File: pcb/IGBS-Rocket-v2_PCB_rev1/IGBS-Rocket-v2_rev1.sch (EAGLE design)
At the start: 157 parts, among them Q1 BC817, Q2 ENC-03, U1 STM32H750VBT6, U2 LD1085D2M-R, U3 LD1085D2M-R, U4 LM317SX/NOPB, U5 MICROSD, U6 ESP-12E/F, U8 LP324DRG4, U9 MCP6V51T-E/MS, Y1 24MHz

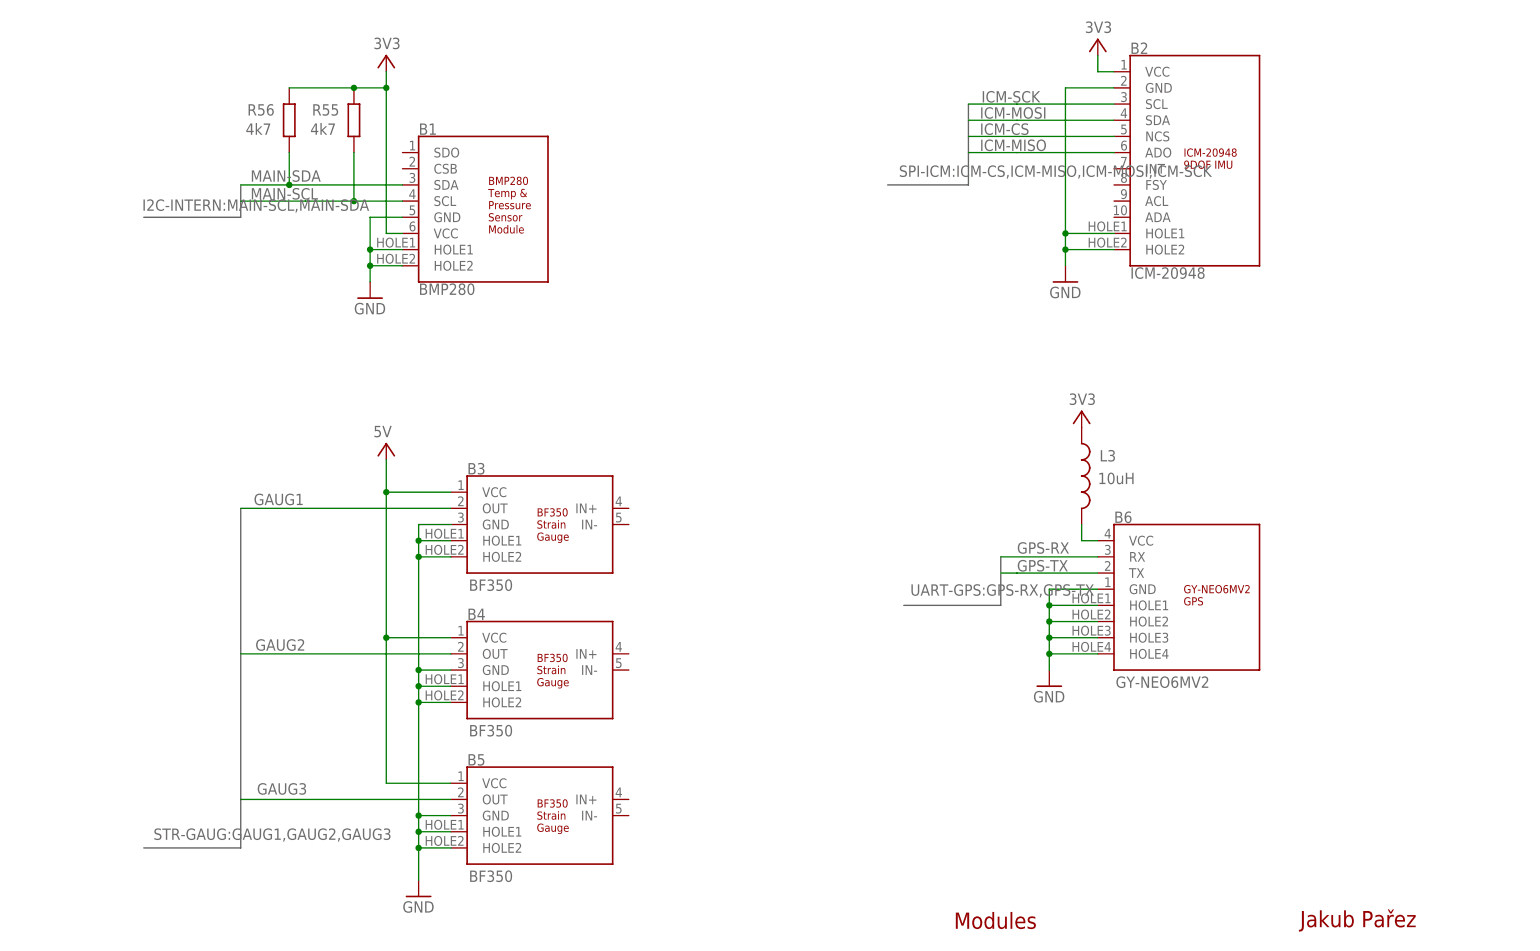
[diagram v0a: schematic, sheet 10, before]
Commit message: * schematics is validated and ready for layout
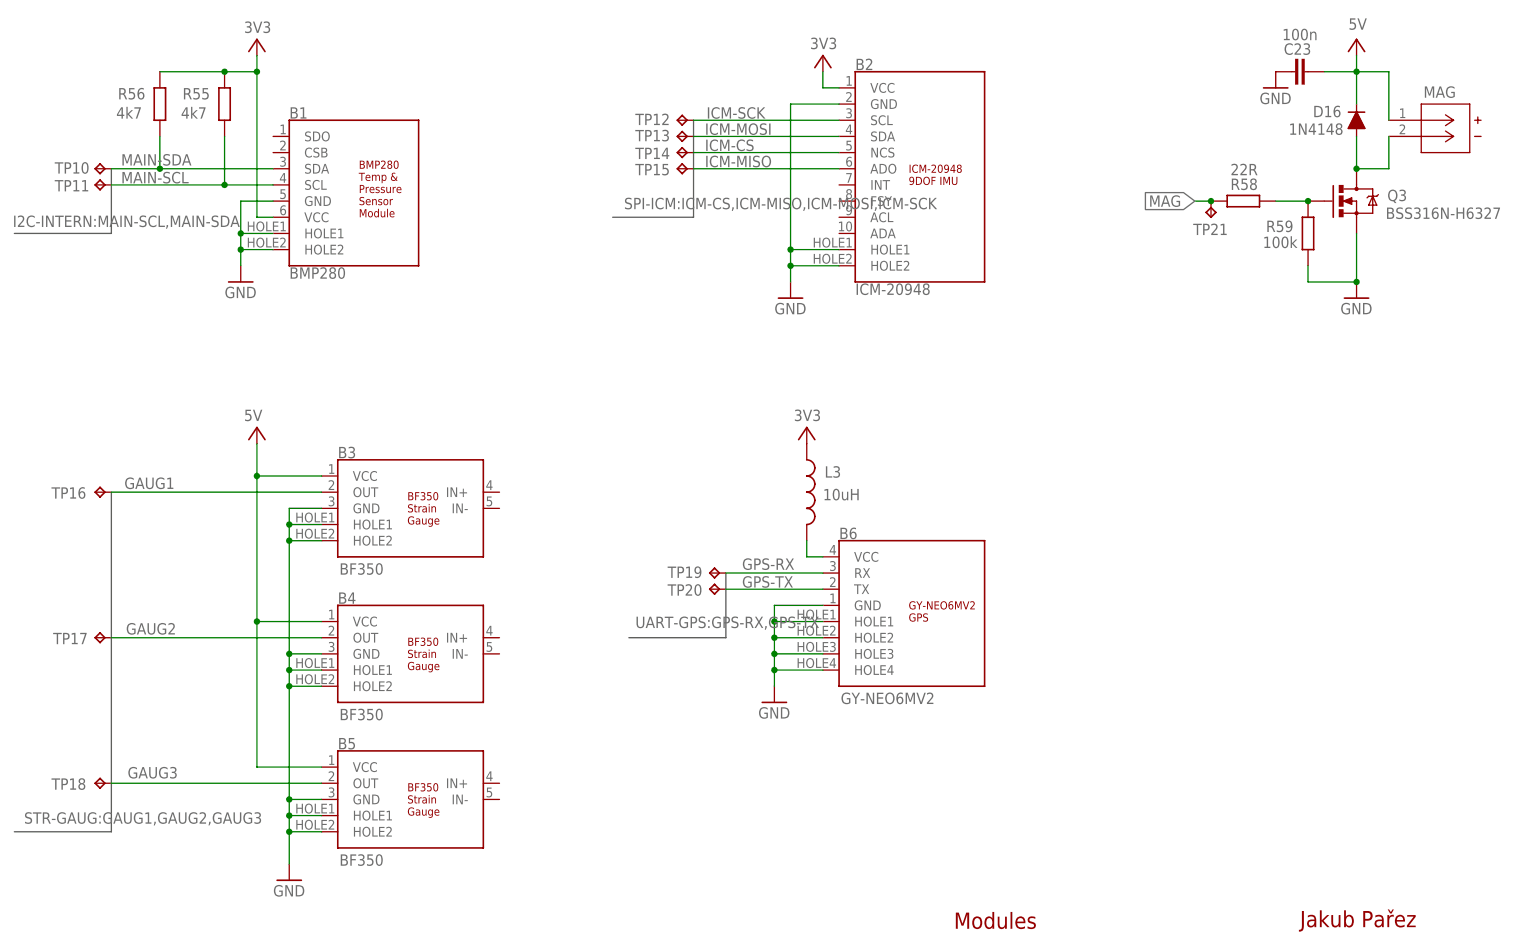
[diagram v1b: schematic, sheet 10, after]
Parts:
- removed BAT, ESP-UART: (no value), pinhead:PINHD-1X2
- removed GYRO: (no value), pinhead:PINHD-1X1
- removed SD-SPI: (no value), pinhead:PINHD-1X4
- added C23: 100n, rcl2:C-EUC0603K
- added D16: 1N4148, SparkFun-DiscreteSemi:DIODESOD123
- added Q3: BSS316N-H6327, SparkFun-DiscreteSemi:MOSFET-NCHANNELBSS123LT1G
- added R58: 22R, rcl2:R-EU_R0603
- added R59: 100k, rcl2:R-EU_R0603
- added TP1: TPB2,54, testpad:TPB2,54
- added TP10, TP11, TP12, TP13, TP14, TP15, TP16, TP17, TP18, TP19, TP2, TP20, TP21, TP3, TP4, TP5, TP6, TP7, TP8, TP9: TPB1,27, testpad:TPB1,27
- MAG: value S3B-XH-A(LF)(SN)CONN_S3B-XH-A(LF)(SN)_JST -> S2B-XH-A(LF)(SN)CONN_S2B-XH-A_JST; device jst-XH2:S3B-XH-A(LF)(SN)CONN_S3B-XH-A(LF)(SN)_JST -> jst-XH2:S2B-XH-A(LF)(SN)CONN_S2B-XH-A_JST
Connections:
- new net N$43: D16.A, MAG.2, Q3.D
- new net N$44: Q3.G, R58.2, R59.2
- net 5V: now also C23.1, D16.C
- net ANG-RATE: now also TP9.TP; no longer GYRO.1
- net BAT: now also TP1.TP; no longer BAT.1
- net ESP-RX: now also TP8.TP; no longer ESP-UART.2
- net ESP-TX: now also TP7.TP; no longer ESP-UART.1
- net GAUG1: now also TP16.TP
- net GAUG2: now also TP17.TP
- net GAUG3: now also TP18.TP
- net GND: now also C23.2, Q3.S, R59.1; no longer BAT.2, MAG.3
- net GPS-RX: now also TP19.TP
- net GPS-TX: now also TP20.TP
- net ICM-CS: now also TP14.TP
- net ICM-MISO: now also TP15.TP
- net ICM-MOSI: now also TP13.TP
- net ICM-SCK: now also TP12.TP
- net MAG: now also R58.1, TP21.TP; no longer MAG.2
- net MAIN-SCL: now also TP11.TP
- net MAIN-SDA: now also TP10.TP
- net SD-CLK: now also TP4.TP; no longer SD-SPI.2
- net SD-CS: now also TP2.TP; no longer SD-SPI.4
- net SD-DETECT: now also TP6.TP
- net SD-MISO: now also TP5.TP; no longer SD-SPI.1
- net SD-MOSI: now also TP3.TP; no longer SD-SPI.3
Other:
- note added: "MAGNET"
- moved on the sheet: 5V, B1, B2, B3, B4, B5, B6, L3, R55, R56

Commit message: + PCB - BOM created * minor adjustments to PCB schematics
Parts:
- removed C32, C34, C37: 10u, rcl2:CPOL-EUCT3216
- removed ON-OFF: (no value), switch_btn:255SB
- added C24, C30, C31: 10u, SparkFun-Capacitors:10UF10V10%(0805)
- 3V3, 5V, I2C-AUX, UART-AUX: device pinhead:PINHD-1X2 -> pinhead2:PINHD-1X2
- ADC-AUX, SPI-AUX: device pinhead:PINHD-1X3 -> pinhead2:PINHD-1X3
- C19, C3, C5, C7, C9: device rcl2:CPOL-EUCT3216 -> SparkFun-Capacitors:10UF10V10%(0805)
- C2: value 2n2 Y2 -> 10u; device rcl2:C-EUC2220K -> SparkFun-Capacitors:10UF10V10%(0805)
- D14: value 3V6 5uA -> 3V6
- GND-AUX, GPIO-AUX: device pinhead:PINHD-1X4 -> pinhead2:PINHD-1X4
- H1, H2, H3, H4: value MOUNT-PAD-ROUND3.0 -> MOUNT-PAD-ROUND2.8; device holes:MOUNT-PAD-ROUND3.0 -> holes:MOUNT-PAD-ROUND2.8
- PPTC1: value 8A -> 6V/2A
- R11, R12, R13, R14, R19, R20, R21, R22, R23, R24, R25, R26, R27, R28, R29, R44, R45, R46, R47, R54: device rcl2:R-EU_R0805 -> rcl2:R-EU_R0603
- SWD: device pinhead:PINHD-1X6 -> pinhead2:PINHD-1X6
- TP1: device testpad:TPB2,54 -> testpad2:TPB2,54
- TP10, TP11, TP12, TP13, TP14, TP15, TP16, TP17, TP18, TP19, TP2, TP20, TP21, TP3, TP4, TP5, TP6, TP7, TP8, TP9: device testpad:TPB1,27 -> testpad2:TPB1,27
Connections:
- net LED1-RED renamed LED1-BLUE
- net LED2-GREEN renamed LED2-YELLOW
- net LED3-BLUE renamed LED3-RED
- net LED4-ORANGE renamed LED4-WHITE
- removed net N$18: ON-OFF.S, PWR-A.+, PWR-B.1
- net 3V3: now also C31.1, C9.1; no longer C3.+, C37.+
- net 5V: now also C19.1; no longer C19.+
- net BAT: now also C2.1, C3.1, C5.1, C7.1; no longer C5.+, C7.+, C9.+
- net GND: now also C24.2, C3.2, C30.2, C31.2, C5.2, C7.2, C9.2; no longer C3.-, C32.-, C34.-, C37.-, C5.-, C7.-, C9.-
- net N$2: now also PWR-A.+, PWR-B.1; no longer C2.1, ON-OFF.P
- net N$29: now also C19.2; no longer C19.-
- net N$39: now also C24.1, C30.1; no longer C32.+, C34.+
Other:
- moved on the sheet: C2, PPTC1, PWR-A, PWR-B

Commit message: + PCB BOM
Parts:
- C16, C17, C26, C27, C28: device rcl2:C-EUC0603K -> rcl2:C-EUC0805K
- L1, L2, L3: device rcl2:INDUCTOR0603 -> rcl2:INDUCTOR0805
- R53: value 75k -> 59k

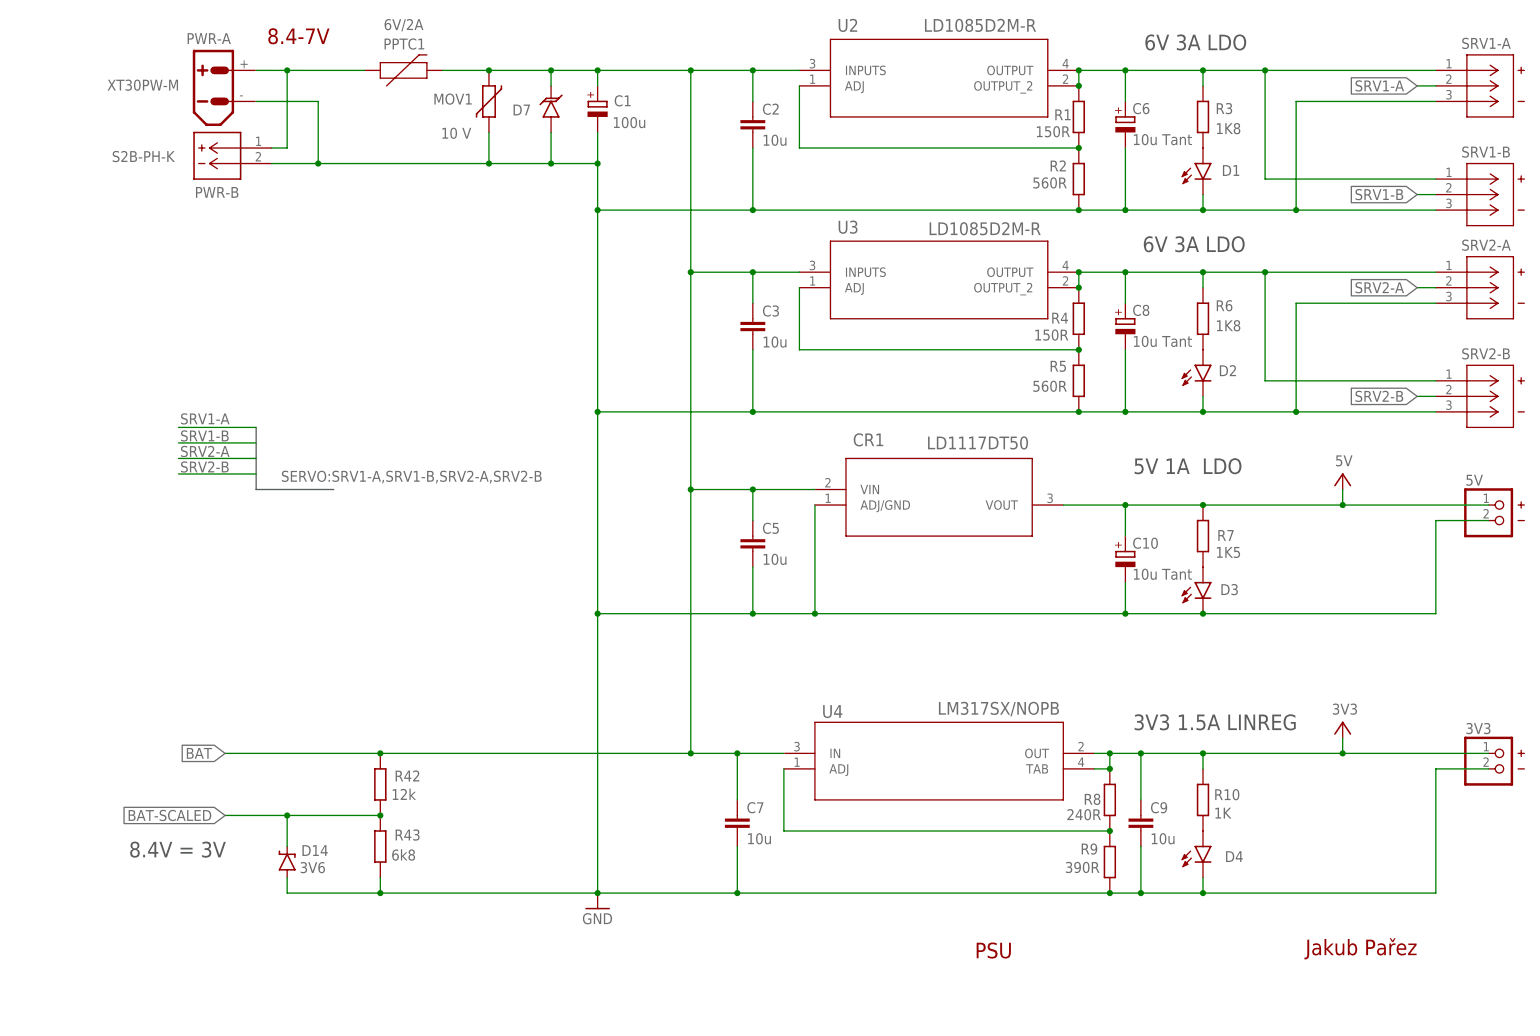
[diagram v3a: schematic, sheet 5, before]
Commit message: * PCB layout 30 % T strain-gauge modules to sch
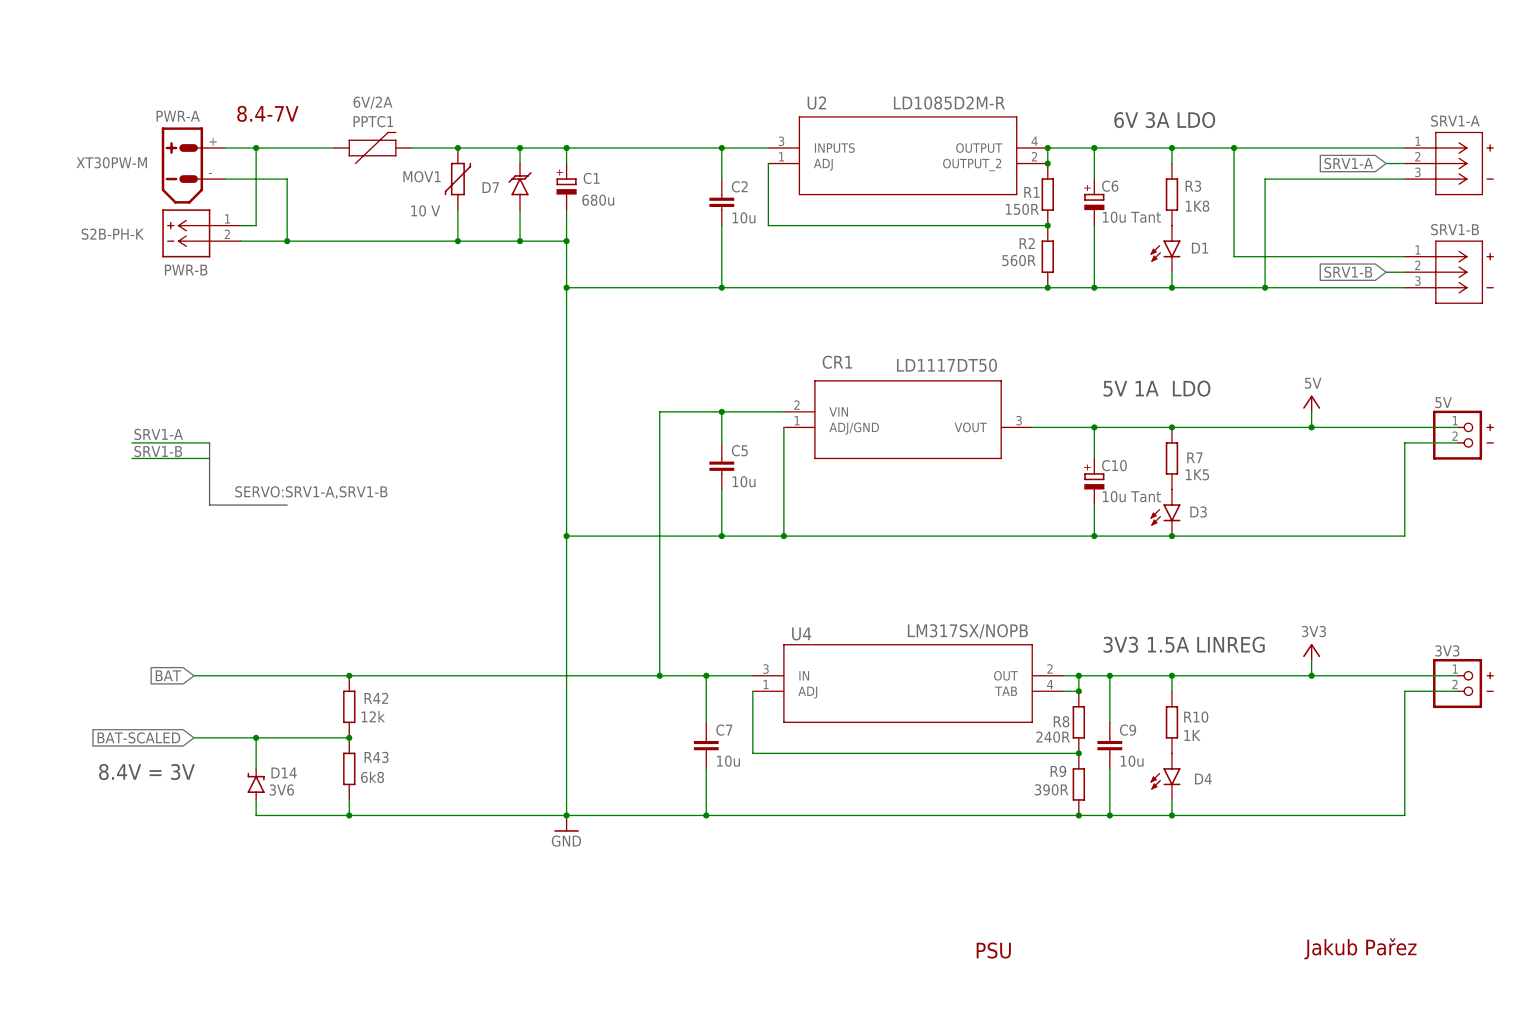
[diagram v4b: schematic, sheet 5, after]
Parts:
- removed C3: 10u, SparkFun-Capacitors:10UF10V10%(0805)
- removed C8: 10u Tant, rcl2:CPOL-EUCT3216
- removed D2: GREEN, leds:LED-GREEN1206
- removed R4: 150R, rcl2:R-EU_R0603
- removed R5: 560R, rcl2:R-EU_R0603
- removed R6: 1K8, rcl2:R-EU_R0603
- removed SRV2-A, SRV2-B: S3B-XH-A(LF)(SN)CONN_S3B-XH-A(LF)(SN)_JST, jst-XH2:S3B-XH-A(LF)(SN)CONN_S3B-XH-A(LF)(SN)_JST
- removed U3: LD1085D2M-R, ldo:LD1085D2M-RD2PAK/A_STM
- added C32: 330u, rcl2:CPOL-EUE2.5-7
- added H5, H6: MOUNT-PAD-ROUND2.8, holes:MOUNT-PAD-ROUND2.8
- added R60, R61: 1K, rcl2:R-EU_R0603
- C1: value 100u -> 680u
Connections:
- removed net 6V-2: C8.+, R4.2, R6.2, SRV2-A.1, SRV2-B.1, U3.OUTPUT, U3.OUTPUT_2
- removed net N$11: R4.1, R5.2, U3.ADJ
- removed net N$12: D2.A, R6.1
- removed net N$20: D15.C, R57.1
- removed net N$24: C21.1, RESET.1
- removed net N$25: C21.2, RESET.3
- removed net N$26: BTN1.1, C22.1
- removed net N$27: BTN1.3, C22.2
- removed net SRV2-A: SRV2-A.2, U1A.PD14
- removed net SRV2-B: SRV2-B.2, U1A.PC7
- new net BTN12: BTN1.2, R14.2, R61.1
- new net N$18: C1.+, C2.1, D7.C, MOV1.1, PPTC1.2, U2.INPUTS
- new net NRST2: R29.2, R60.1, RESET.2
- net ANG-RATE: now also D15.C, R57.1
- net BAT: no longer C1.+, C2.1, C3.1, D7.C, MOV1.1, PPTC1.2, U2.INPUTS, U3.INPUTS
- net BTN1: now also C22.1, R61.2; no longer BTN1.2, R14.2
- net GND: now also C21.2, C22.2, C32.-, H5.MOUNT, H6.MOUNT; no longer C3.2, C8.-, D2.C, R5.1, SRV2-A.3, SRV2-B.3
- net N$39: now also C32.+
- net NRST: now also C21.1, R60.2; no longer R29.2, RESET.2
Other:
- moved on the sheet: 3V3, 5V, BTN1, C1, C10, C2, C21, C22, C5, C6, C7, C9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

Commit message: + PCB schematic is DONE + BOM (Mouser) is DONE
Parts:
- removed B3, B4, B5: BF350, modules:BF350
- removed U4: LM317SX/NOPB, linreg:LM317SX/NOPBTS3B_TEX
- added C3, C35, C40: 100n, rcl2:C-EUC0603K
- added C34, C37, C38, C39, C41, C42, C43, C8: 1u, rcl2:C-EUC0603K
- added CR2, CR3, CR4: TS4040DILT-2.5, ref:TL431QDBZR,215SOT23_TO-236AB_NEX
- added CR5: AZ2185D, ldo:AZ2185D
- added D2: 3V6, SparkFun-DiscreteSemi:DIODE-ZENER16V
- added IC1, IC2, IC3: NCV21872DR2G, opamps:LM358D
- added L4: 10uH, rcl2:INDUCTOR0805
- added R4, R68, R77: 500k, trimmer:PVG3A103C01R00RES_C01R00
- added R5, R69, R78: 10k, rcl2:R-EU_R0603
- added R6, R62, R63, R70, R71, R72, R79, R80, R81: 360R, rcl2:R-EU_R0603
- added R64, R66, R73, R75, R82, R84: 470k, rcl2:R-EU_R0603
- added R65, R74, R83: 20k, rcl2:R-EU_R0603
- added R67, R76, R85: 330R, rcl2:R-EU_R0603
- added SG1, SG2, SG3: S3B-XH-A, jst-XH2:S2B-XH-A(LF)(SN)CONN_S2B-XH-A_JST
- C30: value 10u -> 1u; device SparkFun-Capacitors:10UF10V10%(0805) -> rcl2:C-EUC0603K
- CR1: device ldo:LD1117DT50TRDPAK_STM -> ldo:LD1117DT50TR
- U2: value LD1085D2M-R -> LM317BD2TG; device ldo:LD1085D2M-RD2PAK/A_STM -> linreg:LM317BD2TG
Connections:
- removed net GAUG1: B3.OUT, TP16.TP, U1A.PC5
- removed net GAUG2: B4.OUT, TP17.TP, U1A.PB0
- removed net GAUG3: B5.OUT, TP18.TP, U1A.PB1
- new net ANG-RATE2: C28.2, R53.1, R57.2, U9P.OUT
- new net N$11: R5.2, R6.1, SG1.1
- new net N$12: C8.2, IC1A.+IN, R62.1, R63.2
- new net N$20: R69.2, R70.1, SG2.1
- new net N$24: IC1A.-IN, R5.1, R64.2
- new net N$25: IC1A.OUT, R64.1, R65.2
- new net N$26: IC1B.-IN, R65.1, R66.2
- new net N$53: C34.2, IC1B.+IN, R4.2
- new net N$54: CR2.1, R4.1, R63.1, R67.1, SG1.2
- new net N$55: C37.2, IC2A.+IN, R71.1, R72.2
- new net N$56: IC2A.-IN, R69.1, R73.2
- new net N$57: IC2A.OUT, R73.1, R74.2
- new net N$58: IC2B.-IN, R74.1, R75.2
- new net N$60: C39.2, IC2B.+IN, R68.2
- new net N$61: CR3.1, R68.1, R72.1, R76.1, SG2.2
- new net N$62: R78.2, R79.1, SG3.1
- new net N$63: C41.2, IC3A.+IN, R80.1, R81.2
- new net N$64: IC3A.-IN, R78.1, R82.2
- new net N$65: IC3A.OUT, R82.1, R83.2
- new net N$66: IC3B.-IN, R83.1, R84.2
- new net N$68: C43.2, IC3B.+IN, R77.2
- new net N$69: CR4.1, R77.1, R81.1, R85.1, SG3.2
- new net SG1: C30.2, IC1B.OUT, R66.1, TP16.TP, U1A.PC5
- new net SG2: C38.2, IC2B.OUT, R75.1, TP17.TP, U1A.PB0
- new net SG3: C42.2, IC3B.OUT, R84.1, TP18.TP, U1A.PB1
- net 3V3: now also D2.C, L4.2, U2.OUT, U8A.-, U8B.-, U8C.-, U8D.-; no longer R44.2, R45.2, R46.2, R47.2, U4.OUT, U4.TAB, U8G$1.-, U8G$2.-, U8G$3.-, U8G$4.-
- net 5V: now also C3.2, C35.2, C40.2, IC1P.V+, IC2P.V+, IC3P.V+, R67.2, R76.2, R85.2, U8P.VCC, U9P.VCC; no longer B3.VCC, B4.VCC, B5.VCC, U8G$5.VCC, U9G$1.VCC
- net 6V-1: now also CR5.VOUT; no longer U2.OUTPUT, U2.OUTPUT_2
- net ANG-RATE: now also D2.A; no longer C28.2, R53.1, R57.2, U9G$1.OUT
- net BAT: now also U2.IN; no longer U4.IN
- net GND: now also C3.1, C30.1, C34.1, C35.1, C37.1, C38.1, C39.1, C40.1, C41.1, C42.1, C43.1, C8.1, CR2.2, CR2.3, CR3.2, CR3.3, CR4.2, CR4.3, IC1P.V-, IC2P.V-, IC3P.V-, R4.3, R6.2, R62.2, R68.3, R70.2, R71.2, R77.3, R79.2, R80.2, U8P.GND, U9P.GND; no longer B3.GND, B3.HOLE1, B3.HOLE2, B4.GND, B4.HOLE1, B4.HOLE2, B5.GND, B5.HOLE1, B5.HOLE2, C30.2, U8G$5.GND, U9G$1.GND
- net N$15: now also U2.ADJ; no longer U4.ADJ
- net N$18: now also CR5.VIN; no longer U2.INPUTS
- net N$34: now also U8D.OUT; no longer U8G$4.OUT
- net N$35: now also U8C.OUT; no longer U8G$3.OUT
- net N$36: now also U8B.OUT; no longer U8G$2.OUT
- net N$37: now also U8A.OUT; no longer U8G$1.OUT
- net N$38: now also U8A.+; no longer U8G$1.+
- net N$39: no longer C30.1
- net N$40: now also U8B.+; no longer U8G$2.+
- net N$41: now also U8C.+; no longer U8G$3.+
- net N$42: now also U8D.+; no longer U8G$4.+
- net N$46: now also U9P.+; no longer U9G$1.+
- net N$51: now also U9P.-; no longer U9G$1.-
- net N$9: now also CR5.ADJ/GND; no longer U2.ADJ
- net VCC: now also L4.1, R44.2, R45.2, R46.2, R47.2
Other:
- note added: "GAIN = 6.9 OUTPUT = 1.35 +- (0.2 * 6.9) V RANGE = 0 - 2.73 V"
- note added: "Modules + Magnet"
- note added: "Strain Gauges"
- note removed: "GAIN = 7.82 INPUT = 1.35V +- 200 mV"
- note removed: "Modules"
- note removed: "STRAIN GAUGES"
